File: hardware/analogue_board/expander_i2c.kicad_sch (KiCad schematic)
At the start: 45 parts, among them J701 Button / switch / encoder hol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, J702 Qwiic SM04B-SRSS-TB, J703 I2C holes for a wired display, J704 WS2812 chain holes, U701 TCA9555PWR, U702 M24C64-RMN6TP, U703 SN74AHCT1G125DBVR

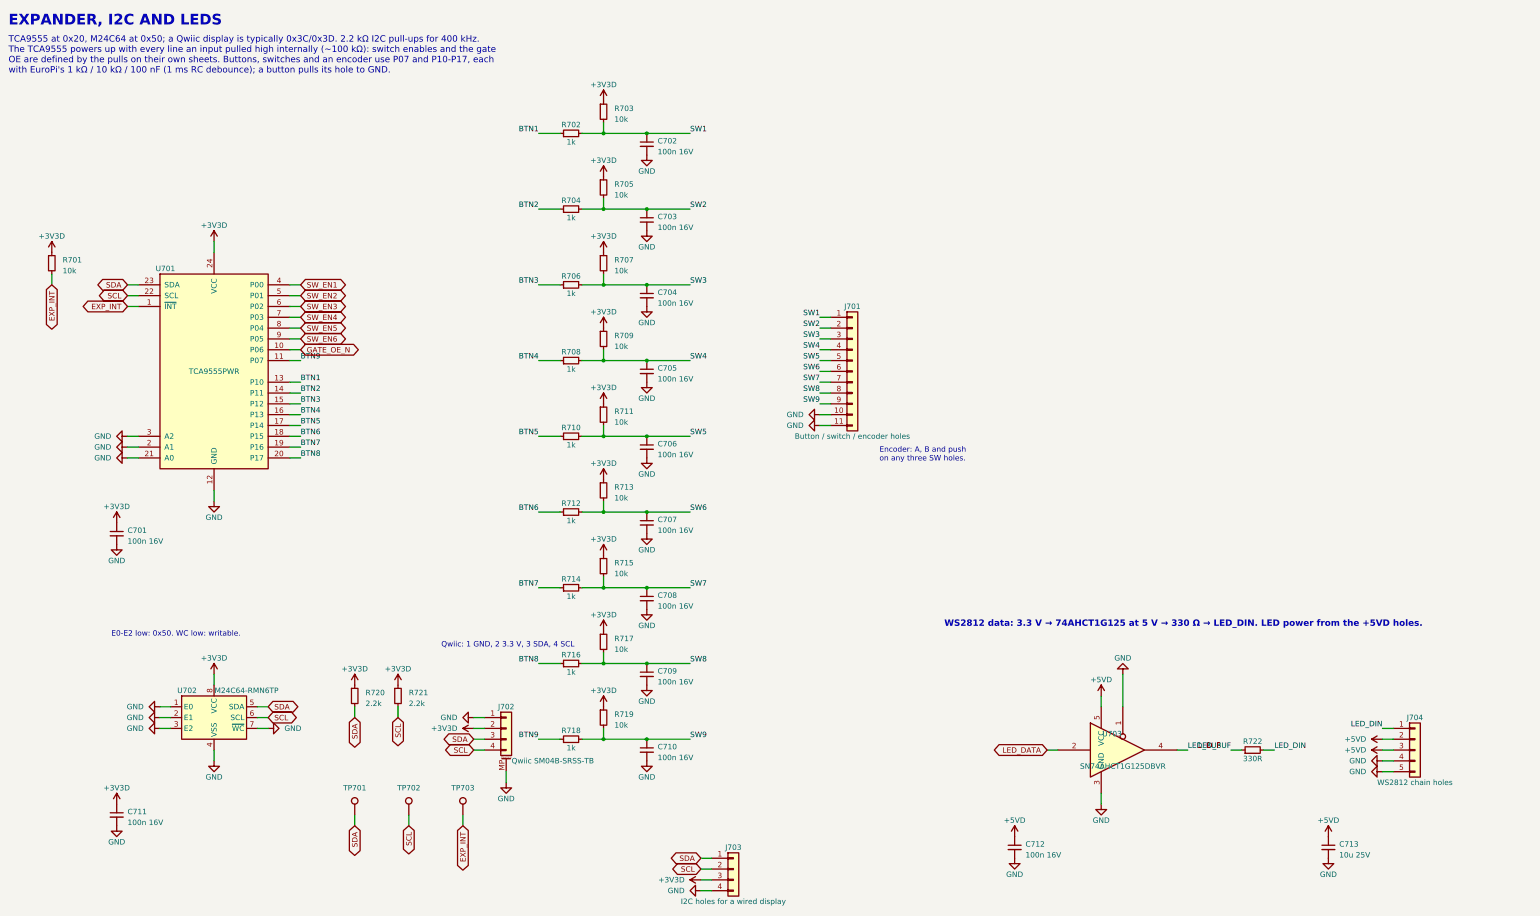
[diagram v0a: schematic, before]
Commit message: Analogue board: block review applied, TRS MIDI, ESP32-P4 support
Checkpoint 1 schematic rebuilt after a block-by-block prior-art review
(docs/analogue_board_review/, seven reports and an index).

Schematic:
- Codec: 20 Vpp in and out (15k input feedback; balanced MFB output,
  gain 2.5, 1 nF C0G); ferrite and 5.1 ohm on the codec supplies; VCOM
  decoupled at each input; CODEC_RST to a hole.
- Power: 680 ohm minimum load on +3V3D; buck input ferrite and EN
  divider; SS34 at D201-D203; Q201/JP201 MOD_5V bypass for the ESP32-P4.
- CV in: 15 V TVS at each jack, 1 nF at each ADC input, 1206 outputs.
- CV out: 12k/22k offset with 1 nF, 33k gain; CV7-8 feedback from the
  jack side of the 1k.
- Gates and panel: CS_595 pull-up, GATE_OE_N on J603, 1M wiper
  pull-downs, POT_REF, button RC order, 47 uF at the LED holes.
- New sheet 10: TRS MIDI (Type A), H11L1 in, 5 V buffered out.
- Layout: no overlapping text on any sheet.

ERC 0/0; netlist identical to intent (345 nets); 21 ICs against
datasheets; 17 Extended part types.

Spec v0.4: David's decisions (TVS yes, CV +/-5 V with a +/-10 V
variant, ESP32-P4 accommodated, power header free to move), the
corrections, and a firmware requirements list in section 15.

Co-Authored-By: Claude Opus 5.5 <noreply@anthropic.com>
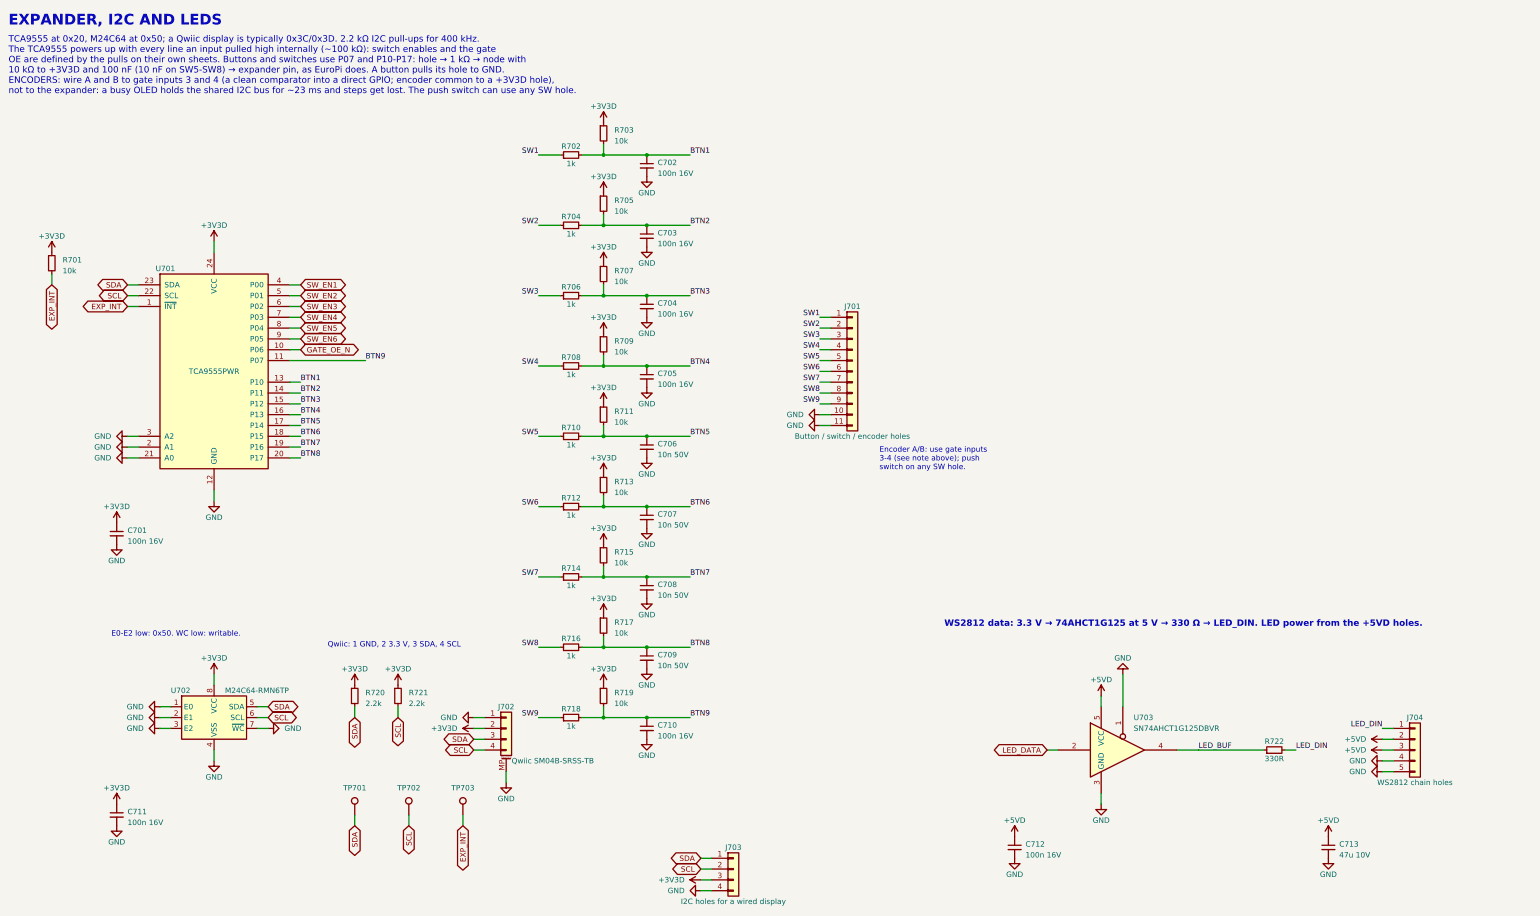
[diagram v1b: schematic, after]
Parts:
- C706, C707, C708, C709: value 100n 16V -> 10n 50V; LCSC C1525 -> C15195; Voltage 16V -> 50V
- C713: value 10u 25V -> 47u 10V; footprint Capacitor_SMD:C_0805_2012Metric -> Capacitor_SMD:C_1206_3216Metric; LCSC C15850 -> C96123; Voltage 25V -> 10V
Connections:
- net BTN1: now also C702.1, R702.2, R703.2; no longer R702.1
- net BTN2: now also C703.1, R704.2, R705.2; no longer R704.1
- net BTN3: now also C704.1, R706.2, R707.2; no longer R706.1
- net BTN4: now also C705.1, R708.2, R709.2; no longer R708.1
- net BTN5: now also C706.1, R710.2, R711.2; no longer R710.1
- net BTN6: now also C707.1, R712.2, R713.2; no longer R712.1
- net BTN7: now also C708.1, R714.2, R715.2; no longer R714.1
- net BTN8: now also C709.1, R716.2, R717.2; no longer R716.1
- net BTN9: now also C710.1, R718.2, R719.2; no longer R718.1
- net SW1: now also R702.1; no longer C702.1, R702.2, R703.2
- net SW2: now also R704.1; no longer C703.1, R704.2, R705.2
- net SW3: now also R706.1; no longer C704.1, R706.2, R707.2
- net SW4: now also R708.1; no longer C705.1, R708.2, R709.2
- net SW5: now also R710.1; no longer C706.1, R710.2, R711.2
- net SW6: now also R712.1; no longer C707.1, R712.2, R713.2
- net SW7: now also R714.1; no longer C708.1, R714.2, R715.2
- net SW8: now also R716.1; no longer C709.1, R716.2, R717.2
- net SW9: now also R718.1; no longer C710.1, R718.2, R719.2
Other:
- note added: "Encoder A/B: use gate inputs 3-4 (see note above); push switch on any SW hole."
- note added: "TCA9555 at 0x20, M24C64 at 0x50; a Qwiic display is typically 0x3C/0x3D. 2.2 kΩ I2C pull-ups for 400 kHz. The TCA9555 powers up with every line an input pulled high internally (~100 kΩ): switch enables and the gate OE are defined by the pulls on their own sheets. Buttons and switches use P07 and P10-P17: hole → 1 kΩ → node with 10 kΩ to +3V3D and 100 nF (10 nF on SW5-SW8) → expander pin, as EuroP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"
- note removed: "Encoder: A, B and push on any three SW holes."
- note removed: "TCA9555 at 0x20, M24C64 at 0x50; a Qwiic display is typically 0x3C/0x3D. 2.2 kΩ I2C pull-ups for 400 kHz. The TCA9555 powers up with every line an input pulled high internally (~100 kΩ): switch enables and the gate OE are defined by the pulls on their own sheets. Buttons, switches and an encoder use P07 and P10-P17, each with EuroPi's 1 kΩ / 10 kΩ / 100 nF (1 ms RC debounce); a button pulls its h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"
- moved on the sheet: C702, C703, C704, C705, C707, C708, C709, C710, R702, R703, R704, R705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

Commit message: Analogue board: checkpoint 3 started; double-sided, floorplan placed
- pcb.py generates analogue_board.kicad_pcb from the netlist: outline,
  JLC 4-layer stack-up, every footprint with nets and schematic links
  (KiCad schematic parity: 0 differences), parked parts beside the board,
  courtyard area budget, DRC and 3D renders of both faces.
- Area budget: the courtyards need 104% of one face before routing, so
  David chose double-sided assembly (JLC Standard PCBA, about $100 more
  per order, to confirm on a quote).
- Floorplan in placement.py: analogue ICs at the top under the modules,
  furthest from the buck; logic below; power bottom right around J201;
  MIDI bottom left; 99 wiring-field holes in three columns lined up with
  the edge-strip positions, each group beside its circuit.
- Library: module socket courtyards cover only their header rows; the
  wiring holes get their own footprint with a one-pitch courtyard.
- Spec records the decision, the floorplan and David's answers: 11 mm to
  the deck in 10HP (deck parts 2 mm at most); holes tinned both faces.

Co-Authored-By: Claude Opus 5.5 <noreply@anthropic.com>
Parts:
- J701: footprint Connector_PinHeader_2.54mm:PinHeader_1x11_P2.54mm_Vertical -> analogue_board:WiringHoles_1x11
- J703: footprint Connector_PinHeader_2.54mm:PinHeader_1x04_P2.54mm_Vertical -> analogue_board:WiringHoles_1x04
- J704: footprint Connector_PinHeader_2.54mm:PinHeader_1x05_P2.54mm_Vertical -> analogue_board:WiringHoles_1x05
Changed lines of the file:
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@@
 			)
 		)
-		(property "Footprint" "Connector_PinHeader_2.54mm:PinHeader_1x11_P2.54mm_Vertical"
+		(property "Footprint" "analogue_board:WiringHoles_1x11"
 			(at 218.44 101.6 0)
 			(effects
@@
 			)
 		)
-		(property "Footprint" "Connector_PinHeader_2.54mm:PinHeader_1x04_P2.54mm_Vertical"
+		(property "Footprint" "analogue_board:WiringHoles_1x04"
 			(at 190.5 218.44 0)
 			(effects
@@
 			)
 		)
-		(property "Footprint" "Connector_PinHeader_2.54mm:PinHeader_1x05_P2.54mm_Vertical"
+		(property "Footprint" "analogue_board:WiringHoles_1x05"
 			(at 350.52 190.5 0)
 			(effects

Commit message: Analogue board: first-pass placement; space reclaimed; four wiring banks
- autoplace.py places every unanchored part as close as it fits to the
  pins it connects to: decoupling capacitors at their pin, chains growing
  from their ICs, the buck's loop kept on one face. All 430 parts placed;
  DRC courtyards clean, schematic parity clean, heights checked (<= 2.5 mm
  under the modules, <= 8 mm in the USB keep-outs).
- Space reclaimed (David): Teensy socket without holes for its unused
  far-end pins 20-28 (headers 1x19 + 1x20); right strip (10HP only) without
  holes at 11-15 and 26-30, and outer hole only at 10, 16, 31. checks.py
  lets a project footprint omit only pins the netlist leaves unconnected.
- 74HCT595 in TSSOP-16 (74HCT595PW, C99710, same pinout) sideways in the
  right channel; vertical Qwiic socket (BM04B-SRSS-TB, C160390) below the
  modules, its cable straight up (the side-entry plug had no clear run).
- Wiring field as four mixed banks (David): each quarter of the board has
  some of every channel type, 50/50 left and right, jack-detect holes
  beside their inputs; wiring.py holds the plan, schematic and placement
  both read it. 94 holes.
- Reference designators off the silkscreen for passives and hole groups.

Co-Authored-By: Claude Opus 5.5 <noreply@anthropic.com>
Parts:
- added J711, J713: Holes, left bottom, analogue_board:WiringHoles_1x01, symbol Connector_Generic:Conn_01x01
- added J712: Holes, left top, analogue_board:WiringHoles_1x01, symbol Connector_Generic:Conn_01x01
- added J714: Holes, right top, analogue_board:WiringHoles_1x03, symbol Connector_Generic:Conn_01x03
- added J715: Holes, right middle, analogue_board:WiringHoles_1x03, symbol Connector_Generic:Conn_01x03
- J702: value Qwiic SM04B-SRSS-TB -> Qwiic BM04B-SRSS-TB; footprint Connector_JST:JST_SH_SM04B-SRSS-TB_1x04-1MP_P1.00mm_Horizontal -> Connector_JST:JST_SH_BM04B-SRSS-TB_1x04-1MP_P1.00mm_Vertical; LCSC C160404 -> C160390; MPN SM04B-SRSS-TB(LF)(SN) -> BM04B-SRSS-TB(LF)(SN)
- J710: renamed from J701; value Button / switch / encoder holes -> Holes, left top; footprint analogue_board:WiringHoles_1x11 -> analogue_board:WiringHoles_1x02; symbol Connector_Generic:Conn_01x11 -> Connector_Generic:Conn_01x02
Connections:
- net GND: now also J714.3 (Pin_3), J715.3 (Pin_3); no longer J710.10 (Pin_10), J710.11 (Pin_11)
- net SW2: now also J712.1 (Pin_1); no longer J710.2 (Pin_2)
- net SW3: now also J710.2 (Pin_2); no longer J710.3 (Pin_3)
- net SW4: now also J711.1 (Pin_1); no longer J710.4 (Pin_4)
- net SW5: now also J713.1 (Pin_1); no longer J710.5 (Pin_5)
- net SW6: now also J714.1 (Pin_1); no longer J710.6 (Pin_6)
- net SW7: now also J714.2 (Pin_2); no longer J710.7 (Pin_7)
- net SW8: now also J715.1 (Pin_1); no longer J710.8 (Pin_8)
- net SW9: now also J715.2 (Pin_2); no longer J710.9 (Pin_9)

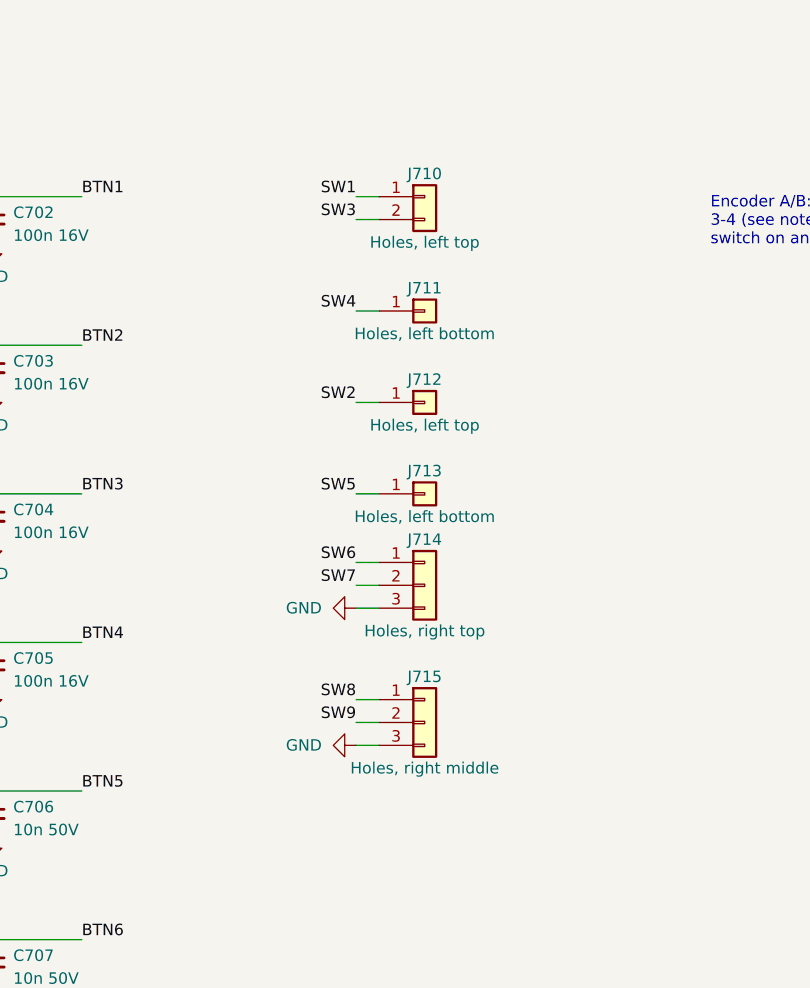
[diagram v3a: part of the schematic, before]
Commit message: Analogue board: bus chips level with their module pins; design rules; trial autoroute
Re-floorplan the centre channel in the order of the module's buses (SPI-A,
SPI-B, I2S, I2C), so the codec is 6 mm from the Pico's I2S pins instead of
38 mm; CV output op-amps move to the top-right corner.

Net classes (0.15/0.15 default, 0.3 power) and an In1 ground plane are
written into the project. autoroute.py runs Freerouting on a copy of the
board to measure routability. Schematic hole groups no longer overlap.

Co-Authored-By: Claude Opus 5.5 <noreply@anthropic.com>
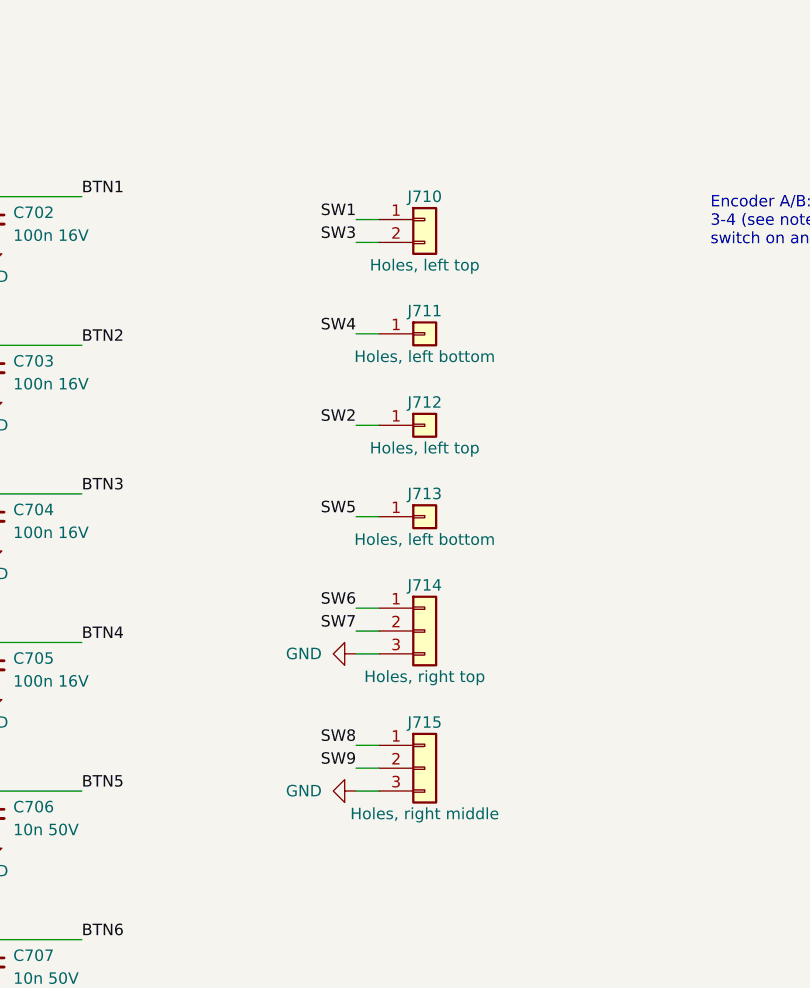
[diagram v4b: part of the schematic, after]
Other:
- moved on the sheet: J710, J711, J712, J713, J714, J715
